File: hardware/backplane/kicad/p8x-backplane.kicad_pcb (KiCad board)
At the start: 4 copper layers, 262 x 128 mm, 33 parts, among them J1 SLOT1, J11 PWR-5V, J2 SLOT2, J3 SLOT3, J4 SLOT4, J5 SLOT5, J6 SLOT6, J7 SLOT7, J8 SLOT8

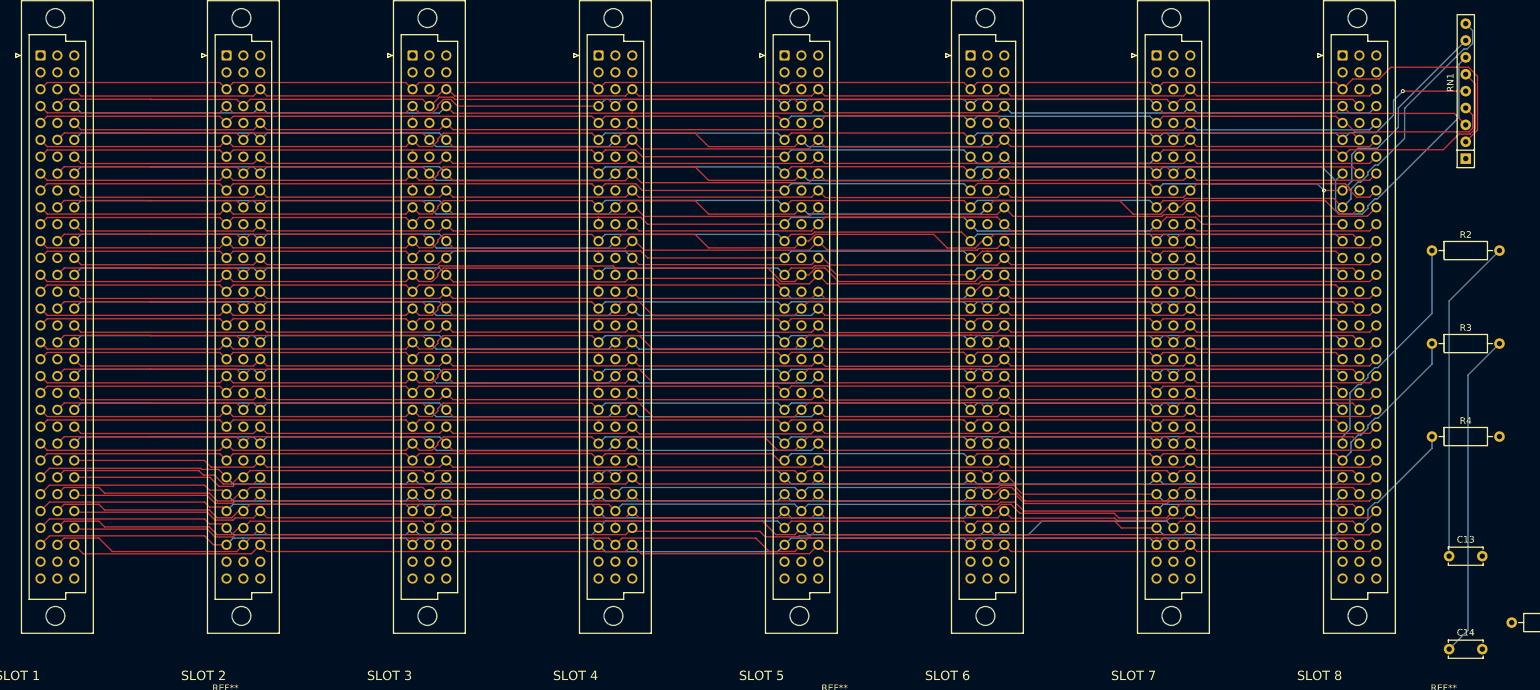
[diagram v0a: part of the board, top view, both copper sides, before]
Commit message: fix(backplane): give CLK/CLKB their own 0.35 mm net class; retry the route
The design doc's clock guard rule was never implemented: every net shared
one 0.13 mm class, so CLKB (the pipeline latch clock) ran 75 mm beside CIN
at 0.44 mm centre-to-centre. gen_backplane.py now puts CLK and CLKB in a
CLOCK net class at 0.35 mm clearance (saved to the .kicad_pro for DRC,
exported as its own DSN class for Freerouting).

Result: worst clock neighbour 1.23 mm (was 0.44), both clocks still the
~230 mm daisy chain (CLK 239, CLKB 228 mm), DRC 0 unconnected, PASS.

0.35 is the ceiling: the DIN pin field (1.55 mm pads, 2.54 mm pitch)
leaves 0.395 mm per side for a track threading two pins. At 0.5 mm the
clocks detoured round the connector ends (~430-450 mm) and left 2
unrouted; 0.8 left 6; 0.38 left 3. A wire_wire-typed Specctra clearance
was not honoured reliably.

A clock track takes a whole pin-row gap, and Freerouting's result depends
on the DSN element order, which changes every placement run; re-routing
the same DSN reproduces a miss exactly. build.sh therefore retries
placement -> route (ROUTE_TRIES 6) until 0 unconnected and the longest
clock <= CLOCK_MAX_MM (300). This build passed on attempt 2.

Docs: design doc section 2, kicad/README, theory doc; the backlog item
moves to BACKLOG-DONE. Schematic relinked (unchanged, ERC 0).

Co-Authored-By: Claude Opus 5.5 <noreply@anthropic.com>
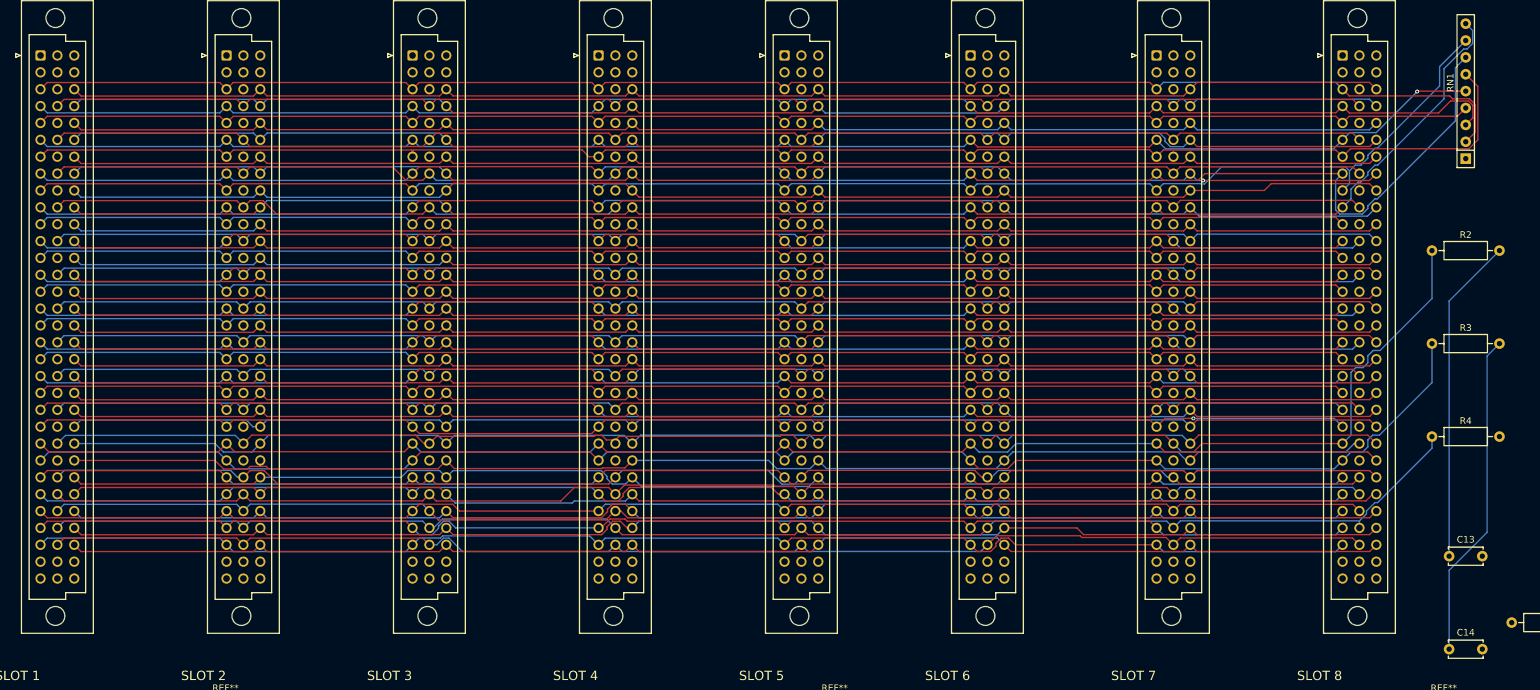
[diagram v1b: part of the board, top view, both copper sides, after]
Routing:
- net D0: track 234.7 -> 229.0 mm
- net D2: track 225.9 -> 221.3 mm
- net D1: track 222.6 -> 226.3 mm
- net IRQ: track 223.1 -> 220.3 mm
- net CLKB: track 225.5 -> 228.1 mm
- net SPARE17: track 204.0 -> 201.9 mm
- net D3: track 225.8 -> 223.8 mm
- net SPARE16: track 203.6 -> 201.9 mm
- net SPARE15: track 204.4 -> 202.7 mm
- net CLK: track 237.6 -> 239.2 mm
- net SH0: track 201.9 -> 203.4 mm
- net D4: track 232.6 -> 234.1 mm
- net BSEL: track 203.6 -> 202.2 mm
- net CIN: track 201.9 -> 203.2 mm
- net DOE0: track 203.2 -> 201.9 mm
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
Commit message: feat(boards): silkscreen labels on every board
Apply the labelling rules to all nine boards: every reference printed
outside every part's courtyard (about 300 sat under their own chip),
the IC type or passive value beside it, function labels on every LED,
switch, jumper and cable connector in the same block as the reference,
and position labels (io DTE/NULL swap jumpers, input switch D0-D7 and
ON=0, bargraph end bits, control JP1 4M/OUT/2M/1M, backplane +5V/GND).

generators/silk_labels.py runs last in every board generator;
check_card.sh fails a board with a hidden reference or one under a
part. Build scripts gain REUSE_ROUTE=1 to re-import the existing
routing for a silkscreen-only change. The backplane mounting holes get
unique refs H1-H6 (six REF** let a routing re-import move one hole onto
another). gen_bom.py shares the chip-type table. All nine boards PASS.

Co-Authored-By: Claude Opus 5.5 <noreply@anthropic.com>
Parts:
- removed REF** (x6): MountingHole_3.2mm_M3, MountingHole_3.2mm_M3
- added H1: MountingHole_3.2mm_M3, MountingHole_3.2mm_M3, F.Cu at (39.3, 6.00)
- added H2: MountingHole_3.2mm_M3, MountingHole_3.2mm_M3, F.Cu at (39.3, 122.0)
- added H3: MountingHole_3.2mm_M3, MountingHole_3.2mm_M3, F.Cu at (131.0, 6.00)
- added H4: MountingHole_3.2mm_M3, MountingHole_3.2mm_M3, F.Cu at (131.0, 122.0)
- added H5: MountingHole_3.2mm_M3, MountingHole_3.2mm_M3, F.Cu at (222.7, 6.00)
- added H6: MountingHole_3.2mm_M3, MountingHole_3.2mm_M3, F.Cu at (222.7, 122.0)
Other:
- board text added: "+5V"
- board text added: "100R"
- board text added: "10K"
- board text added: "150pF"
- board text added: "1K"
- board text added: "470uF"
- board text added: "8X10K"
- board text added: "GND"
- board text added: "POWER IN"
- board text added: "PWR"

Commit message: feat(boards): title block with cottageworker.com on every board
Board rule of 2026-10-26: cottageworker.com on the silkscreen of every
card, beside the board's name and revision. No board carried its name or
revision before. silk_labels.title_block() prints the name + revision
(from the card title; memory REV F, backplane REV A) with the site
beneath, front (right) edge first so it reads with the card installed.
All nine boards rebuilt with the routing reused (silk only); every
check_card PASS.

Co-Authored-By: Claude Opus 5.5 <noreply@anthropic.com>
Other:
- board text added: "P8X BACKPLANE REV A"
- board text added: "cottageworker.com"

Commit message: fix(memory): schematic and title are rev F
The KiCad schematic was drawn from gen_eagle's rev-E netlist (8 KB ROM
decode) and titled REV E, while the board is rev F (6 KB decode). The
rev-F transform moves out of gen_mem.py into mem_revf.py, which the board
and the schematic loader (p8x_card.py) both use. Schematic: "P8X MEMORY
CARD REV F (6K ROM DECODE)", ERC 0, netlist = ours. gen_eagle stays rev E
(Eagle flow frozen). Board pads and tracks unchanged; check_card PASS.

Also the backplane silk title is REV C, matching its schematic (was REV A).

Co-Authored-By: Claude Opus 5.5 <noreply@anthropic.com>
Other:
- board text added: "P8X BACKPLANE REV C"
- board text removed: "P8X BACKPLANE REV A"
